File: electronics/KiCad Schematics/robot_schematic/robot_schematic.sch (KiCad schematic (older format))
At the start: 7 parts, among them M1 Motor_DC, M2 Motor_DC, U2 MP1584EN, U3 MX1508, U4 ESP32-DEVKITC-32D

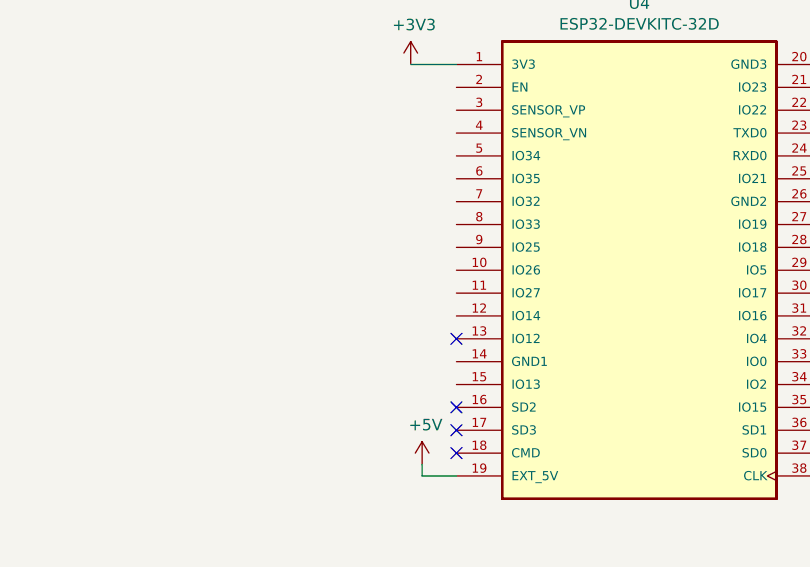
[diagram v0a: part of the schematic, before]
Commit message: Corrected LED on Robot Schematic
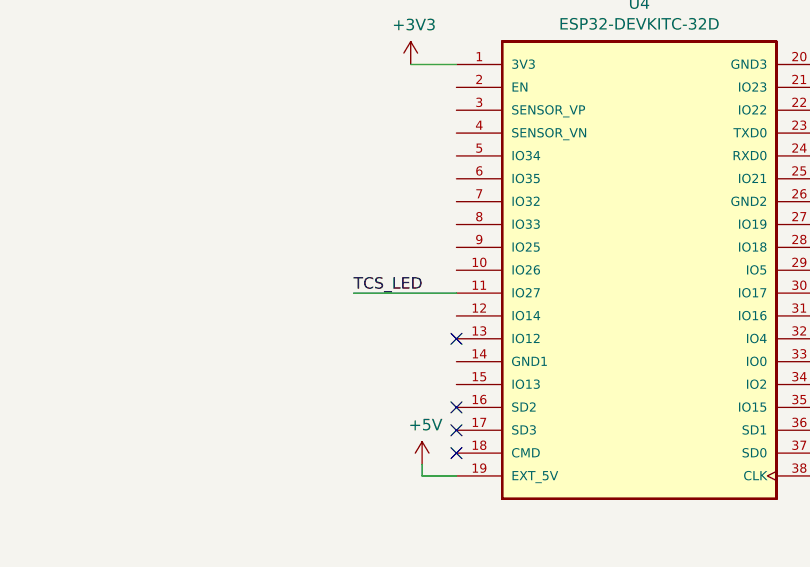
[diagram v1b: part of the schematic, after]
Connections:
- net TCS_LED: now also U4.11 (IO27)
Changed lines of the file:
@@
 	2550 5200 2200 5200
 NoConn ~ 2550 5350
+Wire Wire Line
+	6950 2300 7400 2300
+Text Label 6950 2300 0    50   ~ 0
+TCS_LED
 $EndSCHEMATC
